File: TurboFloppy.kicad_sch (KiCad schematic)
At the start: 20 parts, among them CN1 EXPANSION_PORT, CN2 SOCKET_28PIN, CN3 PIN_HEADER_28PIN, Q1 BC547, U1 8255, U2 74LS30, U4 74LS27, U5 74LS10

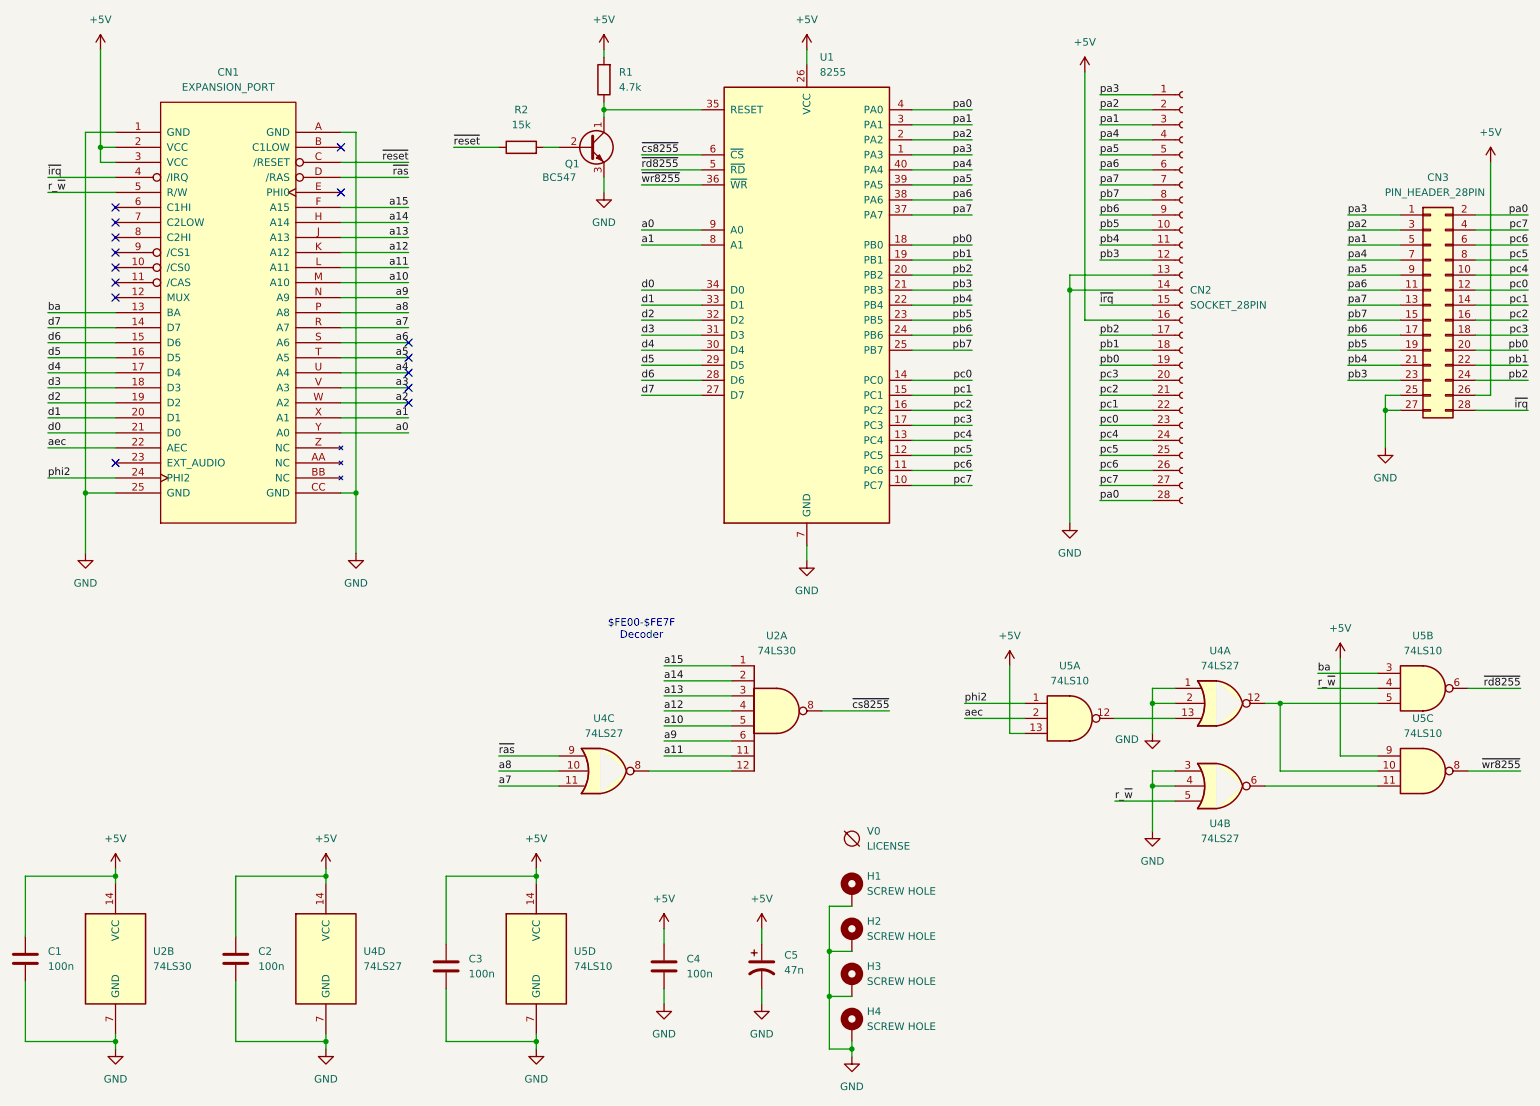
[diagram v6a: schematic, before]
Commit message: Replace all logic with a GAL and make muuuuch smaller
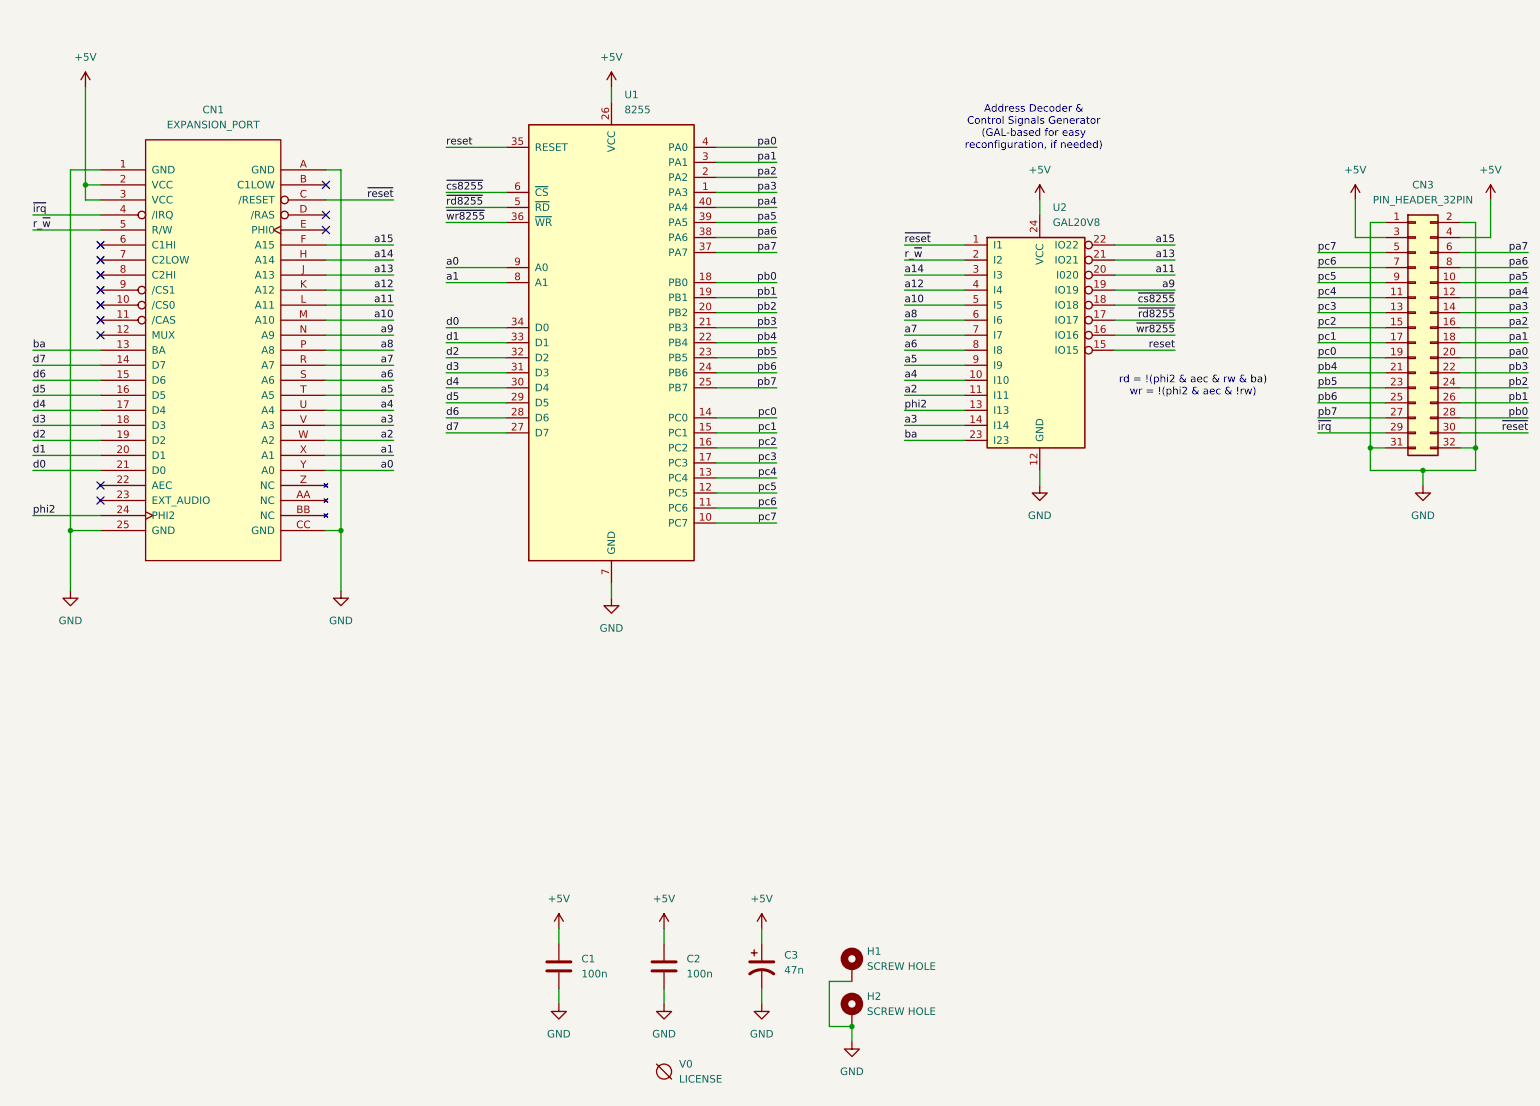
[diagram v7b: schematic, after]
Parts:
- removed C2, C3: 100n, Capacitor_THT:C_Disc_D7.0mm_W2.5mm_P5.00mm, symbol Device:C
- removed CN2: SOCKET_28PIN, Package_DIP:DIP-28_W15.24mm_Socket_LongPads, symbol Connector:Conn_01x28_Socket
- removed CN3: PIN_HEADER_28PIN, Connector_PinHeader_2.54mm:PinHeader_2x14_P2.54mm_Vertical, symbol Connector_Generic:Conn_02x14_Odd_Even
- removed H3, H4: SCREW HOLE, MountingHole:MountingHole_3.2mm_M3_Pad, symbol Mechanical:MountingHole_Pad
- removed Q1: BC547, Package_TO_SOT_THT:TO-92_HandSolder, symbol Transistor_BJT:BC547
- removed R1: 4.7k, Resistor_THT:R_Axial_DIN0207_L6.3mm_D2.5mm_P10.16mm_Horizontal, symbol Device:R
- removed R2: 15k, Resistor_THT:R_Axial_DIN0207_L6.3mm_D2.5mm_P10.16mm_Horizontal, symbol Device:R
- removed U2: 74LS30, Package_DIP:DIP-14_W7.62mm_Socket_LongPads, symbol 74xx:74LS30
- removed U4: 74LS27, Package_DIP:DIP-14_W7.62mm_Socket_LongPads, symbol 74xx:74LS27
- removed U5: 74LS10, Package_DIP:DIP-14_W7.62mm_Socket_LongPads, symbol 74xx:74LS10
- added CN3: PIN_HEADER_32PIN, Connector_PinHeader_2.54mm:PinHeader_2x16_P2.54mm_Vertical, symbol Connector_Generic:Conn_02x16_Odd_Even
- added U2: GAL20V8, Package_DIP:DIP-24_W7.62mm_Socket_LongPads, symbol Logic_Programmable:PAL20L8
- CN1: footprint MODULE -> TurboFloppy:C16_Cart_Conn
- renumbered C4 to C2, C5 to C3
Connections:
- net +5V: now also CN3.3 (Pin_3), CN3.4 (Pin_4), U2.24 (VCC)
- net GND: now also CN3.1 (Pin_1), CN3.2 (Pin_2), CN3.31 (Pin_31), CN3.32 (Pin_32), U2.12 (GND)
- net a10: now also U2.5 (I5)
- net a11: now also U2.20 (I020)
- net a12: now also U2.4 (I4)
- net a13: now also U2.21 (IO21)
- net a14: now also U2.3 (I3)
- net a15: now also U2.22 (IO22)
- net a2: now also U2.11 (I11)
- net a3: now also U2.14 (I14)
- net a4: now also U2.10 (I10)
- net a5: now also U2.9 (I9)
- net a6: now also U2.8 (I8)
- net a7: now also U2.7 (I7)
- net a8: now also U2.6 (I6)
- net a9: now also U2.19 (IO19)
- net ba: now also U2.23 (I23)
- net pa0: now also CN3.20 (Pin_20)
- net pa1: now also CN3.18 (Pin_18)
- net pa2: now also CN3.16 (Pin_16)
- net pa3: now also CN3.14 (Pin_14)
- net pa4: now also CN3.12 (Pin_12)
- net pa5: now also CN3.10 (Pin_10)
- net pa6: now also CN3.8 (Pin_8)
- net pa7: now also CN3.6 (Pin_6)
- net pb0: now also CN3.28 (Pin_28)
- net pb1: now also CN3.26 (Pin_26)
- net pb2: now also CN3.24 (Pin_24)
- net pb3: now also CN3.22 (Pin_22)
- net pb4: now also CN3.21 (Pin_21)
- net pb5: now also CN3.23 (Pin_23)
- net pb6: now also CN3.25 (Pin_25)
- net pb7: now also CN3.27 (Pin_27)
- net pc0: now also CN3.19 (Pin_19)
- net pc1: now also CN3.17 (Pin_17)
- net pc2: now also CN3.15 (Pin_15)
- net pc3: now also CN3.13 (Pin_13)
- net pc4: now also CN3.11 (Pin_11)
- net pc5: now also CN3.9 (Pin_9)
- net pc6: now also CN3.7 (Pin_7)
- net pc7: now also CN3.5 (Pin_5)
- net phi2: now also U2.13 (I13)
- net r_~{w}: now also U2.2 (I2)
- net ~{cs8255}: now also U2.18 (IO18)
- net ~{irq}: now also CN3.29 (Pin_29)
- net ~{rd8255}: now also U2.17 (IO17)
- net ~{reset}: now also CN3.30 (Pin_30), U2.1 (I1)
- net ~{wr8255}: now also U2.16 (IO16)
- net reset: now reaches U1.35 (RESET)
- net reset: now also U2.15 (IO15)
- net aec: no longer names the net of CN1.22 (AEC)
- net ~{ras}: no longer names the net of CN1.D (/RAS)
- no-connect marks 15 -> 12
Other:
- note added: "Address Decoder & Control Signals Generator (GAL-based for easy reconfiguration, if needed)"
- note added: "rd = !(phi2 & aec & rw & ba) wr = !(phi2 & aec & !rw)"
- note removed: "$FE00-$FE7F Decoder"
- moved on the sheet: CN1, H1, H2, U1, V0

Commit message: Final touches
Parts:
- C3: value 47n -> 47u
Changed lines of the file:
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@@
 			)
 		)
-		(property "Value" "47n"
+		(property "Value" "47u"
 			(at 148.59 175.8949 0)
 			(effects
